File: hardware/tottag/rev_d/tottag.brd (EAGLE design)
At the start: 61 x 34.5 mm, 145 parts, among them J1 BAT_HOLE, J2 CON_MICRO_SDDM3AT-SF-PEJM5, J3 MICRO_USB_B_HIROSE_ZX62-B-5PA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, J4 TC2030-JLINK-NL, J5 TC2030-JLINK-NL, T1 HHM1595A1, U1 DW1000, U10 STM32F091CC, U2 FT232RQ, U3 LIS2DW12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

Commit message: added connection to RST pin of nRF
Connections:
- new net !NRF_RST: J4.3, U7.AC13
- net !NRF_CS_SD: now also U7.AD16; no longer U7.AC13
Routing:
- net !NRF_RST: track 0.00 -> 17.4 mm, vias 0 -> 2
- net !NRF_CS_SD: track 9.75 -> 8.67 mm
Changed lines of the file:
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@@
 <wire x1="18.542" y1="10.175" x2="18.527" y2="10.16" width="0.3302" layer="1"/>
 <via x="19.2278" y="18.5166" extent="1-16" drill="0.2032"/>
-<via x="19.3548" y="13.8684" extent="1-16" drill="0.2032"/>
+<via x="19.1516" y="13.6906" extent="1-16" drill="0.2032"/>
 <via x="17.3228" y="17.2466" extent="1-16" drill="0.2032"/>
 <via x="19.2278" y="11.0744" extent="1-16" drill="0.2032"/>
@@
 <via x="21.8948" y="10.4394" extent="1-16" drill="0.2032"/>
 <via x="20.6248" y="12.5984" extent="1-16" drill="0.2032"/>
-<via x="22.5298" y="11.8364" extent="1-16" drill="0.2032"/>
+<via x="22.6568" y="11.8364" extent="1-16" drill="0.2032"/>
 <via x="17.4498" y="8.9154" extent="1-16" drill="0.2032"/>
 <via x="16.6878" y="5.7404" extent="1-16" drill="0.2032"/>
@@
 <via x="17.0186" y="13.925825" extent="1-16" drill="0.2032"/>
 <wire x1="17.0186" y1="13.925825" x2="17.01010625" y2="13.925825" width="0.2032" layer="16"/>
-<contactref element="U7" pad="AC13"/>
-<via x="12.573" y="16.173" extent="1-16" drill="0.2032"/>
-<wire x1="12.446" y1="13.716" x2="12.3698" y2="13.6398" width="0.2032" layer="15"/>
-<wire x1="12.446" y1="15.919" x2="12.446" y2="13.716" width="0.2032" layer="15"/>
-<wire x1="13.589" y1="16.173" x2="15.29265" y2="14.46935" width="0.2032" layer="15"/>
-<wire x1="15.29265" y1="14.46935" x2="16.4751375" y2="14.46935" width="0.2032" layer="15"/>
 <wire x1="16.764" y1="14.17193125" x2="17.01010625" y2="13.925825" width="0.2032" layer="16"/>
 <wire x1="16.764" y1="14.55293125" x2="16.764" y2="14.17193125" width="0.2032" layer="16"/>
-<wire x1="16.4751375" y1="14.46935" x2="17.0186" y2="13.9258875" width="0.2032" layer="15"/>
+<wire x1="17.0186" y1="13.9258875" x2="16.4751375" y2="14.46935" width="0.2032" layer="15"/>
 <wire x1="17.0186" y1="13.9258875" x2="17.0186" y2="13.925825" width="0.2032" layer="15"/>
-<wire x1="12.573" y1="16.173" x2="13.589" y2="16.173" width="0.2032" layer="15"/>
-<wire x1="12.573" y1="16.046" x2="12.446" y2="15.919" width="0.2032" layer="15"/>
-<wire x1="12.573" y1="16.173" x2="12.573" y2="16.046" width="0.2032" layer="15"/>
+<contactref element="U7" pad="AD16"/>
+<via x="13.3682" y="15.677575" extent="1-16" drill="0.2032"/>
+<wire x1="13.3682" y1="14.6382" x2="12.3698" y2="13.6398" width="0.2032" layer="15"/>
+<wire x1="13.323" y1="15.673" x2="13.363625" y2="15.673" width="0.2032" layer="1"/>
+<wire x1="13.3682" y1="15.677575" x2="13.3682" y2="14.6382" width="0.2032" layer="15"/>
+<wire x1="14.576425" y1="14.46935" x2="13.3682" y2="15.677575" width="0.2032" layer="15"/>
+<wire x1="16.4751375" y1="14.46935" x2="14.576425" y2="14.46935" width="0.2032" layer="15"/>
+<wire x1="13.323" y1="15.673" x2="13.363625" y2="15.673" width="0.2032" layer="1"/>
+<wire x1="13.363625" y1="15.673" x2="13.3682" y2="15.677575" width="0.2032" layer="1"/>
 </signal>
 <signal name="!SD_DETECT">
@@
 <wire x1="12.823" y1="15.673" x2="12.86036875" y2="15.71036875" width="0.2032" layer="1"/>
 <via x="12.86036875" y="15.71036875" extent="1-16" drill="0.2032"/>
-<wire x1="12.86036875" y1="15.71036875" x2="13.3858" y2="16.2358" width="0.254" layer="16"/>
-<wire x1="13.3858" y1="16.2358" x2="13.3858" y2="16.97585" width="0.254" layer="16"/>
+<wire x1="12.86036875" y1="15.81196875" x2="13.3858" y2="16.3374" width="0.254" layer="16"/>
+<wire x1="13.3858" y1="16.3374" x2="13.3858" y2="16.97585" width="0.254" layer="16"/>
 <wire x1="18.77185" y1="12.37106875" x2="19.827" y2="11.31591875" width="0.3302" layer="1"/>
 <wire x1="19.827" y1="11.31591875" x2="19.827" y2="10.16" width="0.3302" layer="1"/>
@@
 <wire x1="13.4112" y1="23.0632" x2="10.1092" y2="23.0632" width="0.381" layer="15"/>
 <wire x1="10.1092" y1="23.0632" x2="9.46185" y2="22.41585" width="0.381" layer="15"/>
+<wire x1="12.86036875" y1="15.71036875" x2="12.86036875" y2="15.81196875" width="0.254" layer="16"/>
 </signal>
 <signal name="N$22">
@@
 <wire x1="2.4384" y1="2.4638" x2="5.091" y2="2.4638" width="0.2032" layer="15"/>
 </signal>
+<signal name="!NRF_RST">
+<contactref element="U7" pad="AC13"/>
+<contactref element="J4" pad="3"/>
+<via x="12.573" y="16.173" extent="1-16" drill="0.2032"/>
+<wire x1="12.573" y1="16.173" x2="13.672" y2="16.173" width="0.2032" layer="15"/>
+<via x="26.543" y="10.795" extent="1-16" drill="0.2032"/>
+<wire x1="23.71053125" y1="10.63348125" x2="26.38148125" y2="10.63348125" width="0.2032" layer="15"/>
+<wire x1="22.5711375" y1="11.2268" x2="23.1172125" y2="11.2268" width="0.2032" layer="15"/>
+<wire x1="23.1172125" y1="11.2268" x2="23.71053125" y2="10.63348125" width="0.2032" layer="15"/>
+<wire x1="13.672" y1="16.173" x2="14.89305" y2="14.95195" width="0.2032" layer="15"/>
+<wire x1="26.543" y1="10.795" x2="26.543" y2="10.392425" width="0.2032" layer="1"/>
+<wire x1="26.543" y1="10.392425" x2="26.0985" y2="9.947925" width="0.2032" layer="1"/>
+<wire x1="26.38148125" y1="10.63348125" x2="26.543" y2="10.795" width="0.2032" layer="15"/>
+<wire x1="19.35693125" y1="14.0642625" x2="19.733675" y2="14.0642625" width="0.2032" layer="15"/>
+<wire x1="18.46924375" y1="14.95195" x2="19.35693125" y2="14.0642625" width="0.2032" layer="15"/>
+<wire x1="19.733675" y1="14.0642625" x2="22.5711375" y2="11.2268" width="0.2032" layer="15"/>
+<wire x1="14.89305" y1="14.95195" x2="18.46924375" y2="14.95195" width="0.2032" layer="15"/>
+</signal>
 </signals>

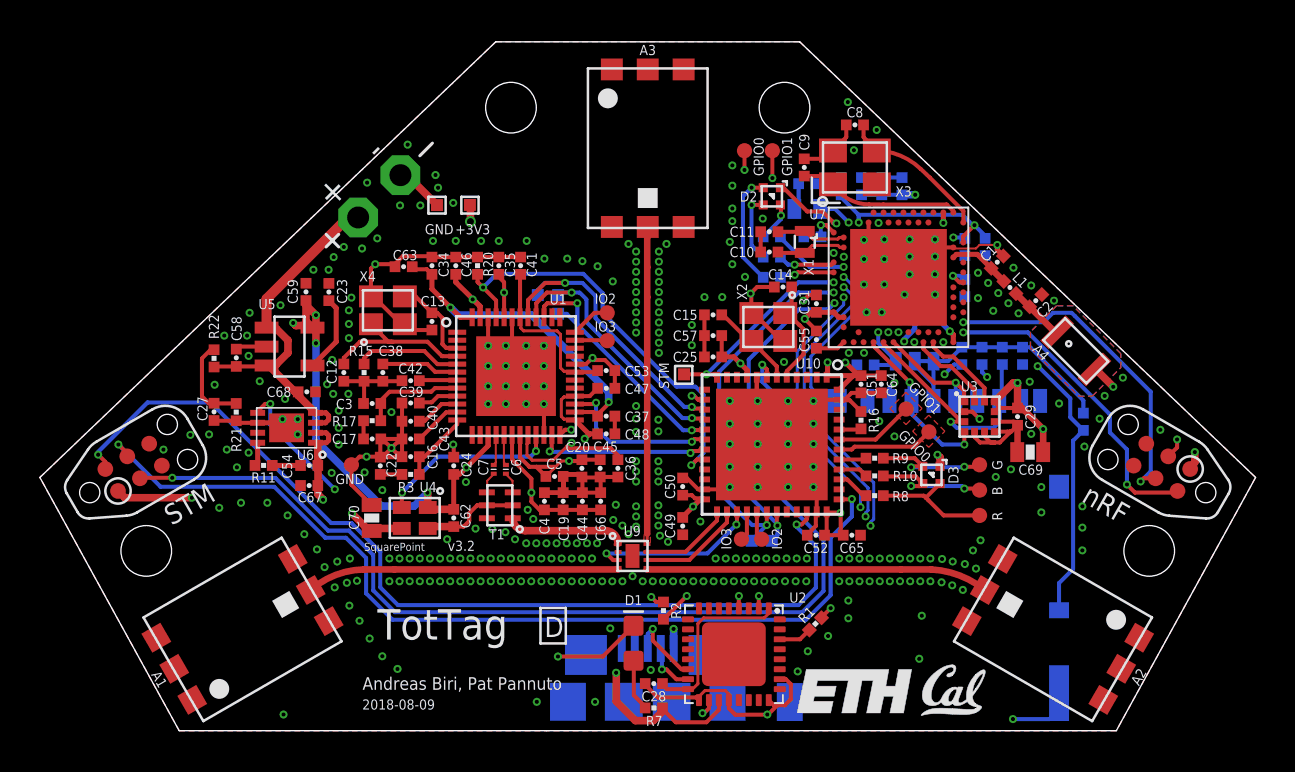
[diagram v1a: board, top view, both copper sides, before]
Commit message: added testpoint for +1V8, optimized power plane, added ground vias, shifted test pads
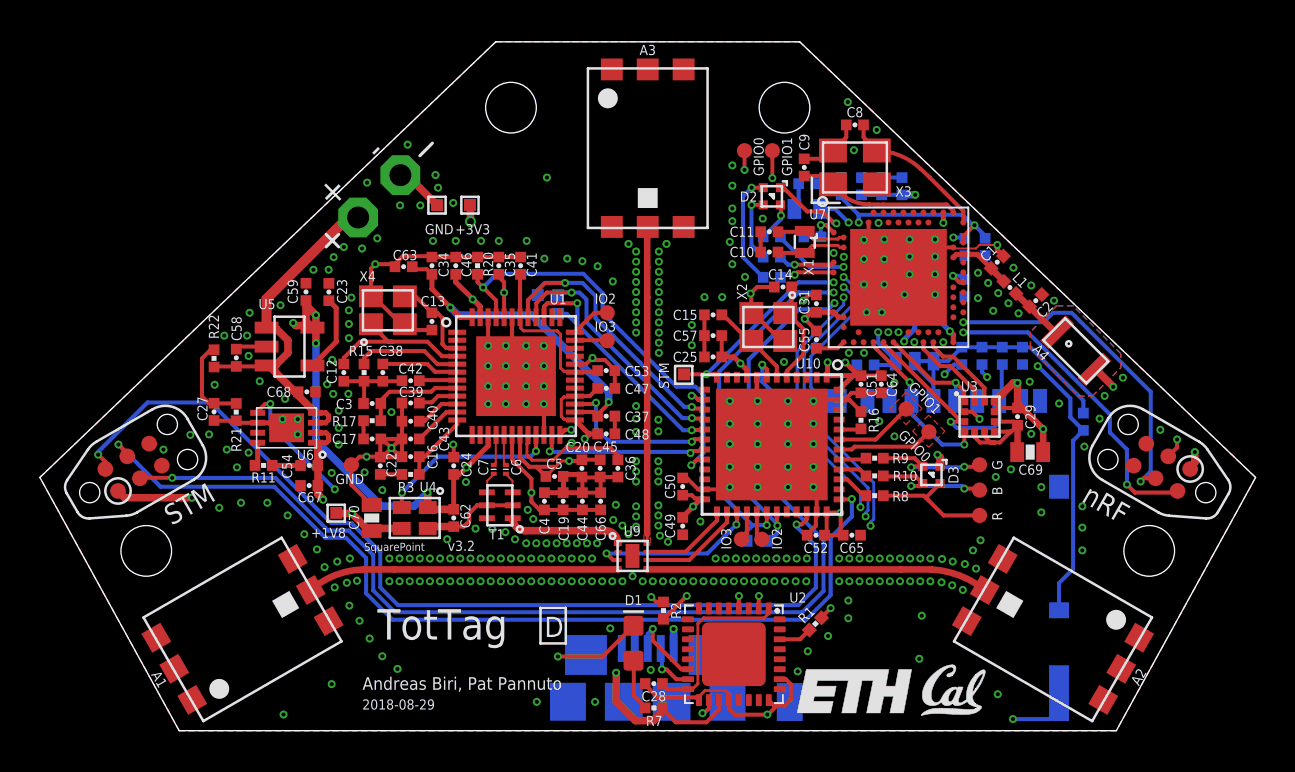
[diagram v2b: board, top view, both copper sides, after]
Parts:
- added +1V8: TPTP06SQ, testpad:TP06SQ
- J1: value BAT_HOLE -> MICRO_USB_B_HIROSE_ZX62-B-5PA(11); device connector:BATTERY_HOLE -> connector:USB_MICRO_B-HIROSE-ZX62-B-5PA(11)
- J3: value MICRO_USB_B_HIROSE_ZX62-B-5PA(11) -> BAT_HOLE; device connector:USB_MICRO_B-HIROSE-ZX62-B-5PA(11) -> connector:BATTERY_HOLE
- moved J1 30.0 mm to (0.00, -3.81), flipped to the bottom, turned to 0 degrees
- moved J3 30.0 mm to (-13.5, 23.0), flipped to the top, turned to 45 degrees
- moved TP1 0.25 mm to (4.95, 5.71)
- moved TP2 0.25 mm to (5.97, 5.71)
- renumbered L6 to L3
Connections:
- net +1V8: now also +1V8.TP
- net D+: now also J1.3; no longer J3.3
- net D-: now also J1.2; no longer J3.2
- net GND: now also J1.5, J3.N; no longer J1.N, J3.5
- net VBAT: now also J3.P; no longer J1.P
- net VUSB: now also J1.1; no longer J3.1
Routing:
- net +1V8: track 32.2 -> 33.0 mm
- net EXT_I2C_SCL: track 18.3 -> 18.8 mm
- net GND: vias 357 -> 360
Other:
- board text added: "2018-08-29"
- board text removed: "2018-08-09"
